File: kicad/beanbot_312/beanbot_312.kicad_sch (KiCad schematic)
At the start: 53 parts, among them M1 P&O2_MEETPUNT, M10 P&O2_RGB_LED, M11 P&O2_RESISTOR, M12 P&O2_MEETPUNT, M13 P&O2_RESISTOR, M14 P&O2_MOSFET, M15 P&O2_RESISTOR, M16 P&O2_ULTRASONE_HC_SR04, M17 P&O2_MEETPUNT, M18 P&O2_MEETPUNT, M19 P&O2_MEETPUNT, M2 P&O2_MEETPUNT, M20 P&O2_MEETPUNT, M21 P&O2_GEWICHTSENSOR2, M22 P&O2_MEETPUNT, M23 P&O2_MEETPUNT, M24 P&O2_MEETPUNT, M25 P&O2_KLEURSENSOR, M26 P&O2_MEETPUNT, M27 P&O2_RELAIS-DP, M28 P&O2_DC-MOTOR, M29 P&O2_RELAIS-DP, M3 P&O2_RESISTOR, M30 P&O2_DC-MOTOR, M31 P&O2_RELAIS-DP, M32 P&O2_DC-MOTOR, M33 P&O2_DIODE, M34 P&O2_DIODE, M35 P&O2_DIODE, M36 P&O2_MEETPUNT, M37 P&O2_MEETPUNT, M38 P&O2_MEETPUNT, M39 P&O2_MEETPUNT, M4 P&O2_MOSFET, M40 P&O2_MEETPUNT, M41 P&O2_MEETPUNT, M42 P&O2_RESISTOR, M43 P&O2_RESISTOR, M44 P&O2_RESISTOR, M45 P&O2_MOSFET, M46 P&O2_MOSFET, M47 P&O2_MOSFET, M48 P&O2_MEETPUNT, M49 P&O2_MEETPUNT, M5 P&O2_RESISTOR, M50 P&O2_MEETPUNT, M51 P&O2_MEETPUNT, M6 P&O2_MEETPUNT, M7 P&O2_RESISTOR, M8 P&O2_MOSFET, M9 P&O2_RESISTOR, U1 P&O2_ARDUINO_MEGA_SHIELD

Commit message: Restore latest version
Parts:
- added M27: P&O2_MEETPUNT, 1_P&O2_lib:P&O2_MEETPUNT, symbol 1_P&O2_lib:P&O2_MEETPUNT
- renumbered M51 to M28, M27 to M29, M28 to M30, M29 to M31, M30 to M32, M31 to M33, M32 to M34, M33 to M35, M34 to M36, M35 to M37, M36 to M38, M37 to M39, M38 to M40, M39 to M41, M40 to M42, M41 to M43, M42 to M44, M43 to M45, M44 to M46, M45 to M47, M46 to M48, M47 to M49, M48 to M50, M49 to M51, M50 to M52
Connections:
- net GND: now also M27.1 (TP)

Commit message: Made outline for pcb
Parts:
- M11, M13, M15, M3, M5, M7, M9: footprint 1_P&O2_lib:P&O2_RES -> 1_P&O2_lib:P&O2_RESISTOR
- SV1: footprint (none) -> 1_P&O2_lib:P&O2_DIP16
- U1: footprint 1_P&O2_lib:P&O2_ARDUINO_MEGA_SHIELD -> (none)
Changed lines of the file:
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@@
       (effects (font (size 1.143 1.143)) (justify left))
     )
-    (property "Footprint" "1_P&O2_lib:P&O2_RES" (id 2) (at 33.02 268.732 0)
+    (property "Footprint" "1_P&O2_lib:P&O2_RESISTOR" (id 2) (at 33.02 268.732 0)
       (effects (font (size 0.508 0.508)) hide)
     )
@@
       (effects (font (size 1.143 1.143)))
     )
-    (property "Footprint" "" (id 2) (at 115.57 189.738 0)
+    (property "Footprint" "1_P&O2_lib:P&O2_DIP16" (id 2) (at 115.57 189.738 0)
       (effects (font (size 0.508 0.508)) hide)
     )
@@
       (effects (font (size 1.143 1.143)))
     )
-    (property "Footprint" "1_P&O2_lib:P&O2_RES" (id 2) (at 85.09 177.038 0)
+    (property "Footprint" "1_P&O2_lib:P&O2_RESISTOR" (id 2) (at 85.09 177.038 0)
       (effects (font (size 0.508 0.508)) hide)
     )
@@
       (effects (font (size 1.143 1.143)) (justify left))
     )
-    (property "Footprint" "1_P&O2_lib:P&O2_RES" (id 2) (at 74.93 244.602 0)
+    (property "Footprint" "1_P&O2_lib:P&O2_RESISTOR" (id 2) (at 74.93 244.602 0)
       (effects (font (size 0.508 0.508)) hide)
     )
@@
       (effects (font (size 1.143 1.143)) (justify left))
     )
-    (property "Footprint" "1_P&O2_lib:P&O2_RES" (id 2) (at 38.1 244.602 0)
+    (property "Footprint" "1_P&O2_lib:P&O2_RESISTOR" (id 2) (at 38.1 244.602 0)
       (effects (font (size 0.508 0.508)) hide)
     )
@@
     (property "Reference" "U1" (id 0) (at 97.155 46.99 0))
     (property "Value" "P&O2_ARDUINO_MEGA_SHIELD" (id 1) (at 97.155 49.53 0))
-    (property "Footprint" "1_P&O2_lib:P&O2_ARDUINO_MEGA_SHIELD" (id 2) (at 49.53 149.86 0)
+    (property "Footprint" "" (id 2) (at 49.53 149.86 0)
       (effects (font (size 1.27 1.27)) hide)
     )
@@
       (effects (font (size 1.143 1.143)) (justify left))
     )
-    (property "Footprint" "1_P&O2_lib:P&O2_RES" (id 2) (at 69.85 268.732 0)
+    (property "Footprint" "1_P&O2_lib:P&O2_RESISTOR" (id 2) (at 69.85 268.732 0)
       (effects (font (size 0.508 0.508)) hide)
     )
@@
       (effects (font (size 1.143 1.143)) (justify left))
     )
-    (property "Footprint" "1_P&O2_lib:P&O2_RES" (id 2) (at 110.49 244.602 0)
+    (property "Footprint" "1_P&O2_lib:P&O2_RESISTOR" (id 2) (at 110.49 244.602 0)
       (effects (font (size 0.508 0.508)) hide)
     )
@@
       (effects (font (size 1.143 1.143)) (justify left))
     )
-    (property "Footprint" "1_P&O2_lib:P&O2_RES" (id 2) (at 105.41 268.732 0)
+    (property "Footprint" "1_P&O2_lib:P&O2_RESISTOR" (id 2) (at 105.41 268.732 0)
       (effects (font (size 0.508 0.508)) hide)
     )
@@
     )
     (path "/14482988-d976-4b64-84c3-34b19aa3c080"
-      (reference "M3") (unit 1) (value "P&O2_RESISTOR") (footprint "1_P&O2_lib:P&O2_RES")
+      (reference "M3") (unit 1) (value "P&O2_RESISTOR") (footprint "1_P&O2_lib:P&O2_RESISTOR")
     )
     (path "/6c971ce3-1431-46f9-8da7-bbee1109d8c7"
@@
     )
     (path "/89a9d6ea-785f-4361-8a21-ea3d7a427841"
-      (reference "M5") (unit 1) (value "P&O2_RESISTOR") (footprint "1_P&O2_lib:P&O2_RES")
+      (reference "M5") (unit 1) (value "P&O2_RESISTOR") (footprint "1_P&O2_lib:P&O2_RESISTOR")
     )
     (path "/27fa6b28-2749-4951-8431-a85c04f7dccf"
@@
     )
     (path "/a9fbfec0-73fe-4272-aeae-3ce0e9053838"
-      (reference "M7") (unit 1) (value "P&O2_RESISTOR") (footprint "1_P&O2_lib:P&O2_RES")
+      (reference "M7") (unit 1) (value "P&O2_RESISTOR") (footprint "1_P&O2_lib:P&O2_RESISTOR")
     )
     (path "/1e4ba2ce-8f73-4698-94a3-6f7c8d2840a2"
@@
     )
     (path "/760a86ab-c275-4512-b55b-15f683b8a6dd"
-      (reference "M9") (unit 1) (value "P&O2_RESISTOR") (footprint "1_P&O2_lib:P&O2_RES")
+      (reference "M9") (unit 1) (value "P&O2_RESISTOR") (footprint "1_P&O2_lib:P&O2_RESISTOR")
     )
     (path "/f3747c8d-50dd-4b9f-b48c-f49fc331b26d"
@@
     )
     (path "/495f9e22-4870-42e2-8c9f-b89669711850"
-      (reference "M11") (unit 1) (value "P&O2_RESISTOR") (footprint "1_P&O2_lib:P&O2_RES")
+      (reference "M11") (unit 1) (value "P&O2_RESISTOR") (footprint "1_P&O2_lib:P&O2_RESISTOR")
     )
     (path "/83e7bd01-8410-4616-9457-7ee77c468abc"
@@
     )
     (path "/f3adaaab-422c-4953-8879-b08863ca4923"
-      (reference "M13") (unit 1) (value "P&O2_RESISTOR") (footprint "1_P&O2_lib:P&O2_RES")
+      (reference "M13") (unit 1) (value "P&O2_RESISTOR") (footprint "1_P&O2_lib:P&O2_RESISTOR")
     )
     (path "/ca63cb53-2ff8-4934-af06-3de3b0c74780"
@@
     )
     (path "/baab9130-8189-4ac5-bff7-a58ac8995f3b"
-      (reference "M15") (unit 1) (value "P&O2_RESISTOR") (footprint "1_P&O2_lib:P&O2_RES")
+      (reference "M15") (unit 1) (value "P&O2_RESISTOR") (footprint "1_P&O2_lib:P&O2_RESISTOR")
     )
     (path "/524c9472-4b27-4e81-93fa-4ac570aaef19"
@@
     )
     (path "/31e61e3b-86e2-42f7-90c4-159698048ccb"
-      (reference "SV1") (unit 1) (value "P&O2_LCD") (footprint "")
+      (reference "SV1") (unit 1) (value "P&O2_LCD") (footprint "1_P&O2_lib:P&O2_DIP16")
     )
     (path "/93bc6bf3-eadd-4f0c-82a1-9da79f283ddb"
-      (reference "U1") (unit 1) (value "P&O2_ARDUINO_MEGA_SHIELD") (footprint "1_P&O2_lib:P&O2_ARDUINO_MEGA_SHIELD")
-    )
-  )
+      (reference "U1") (unit 1) (value "P&O2_ARDUINO_MEGA_SHIELD") (footprint "")
+    )
+  )

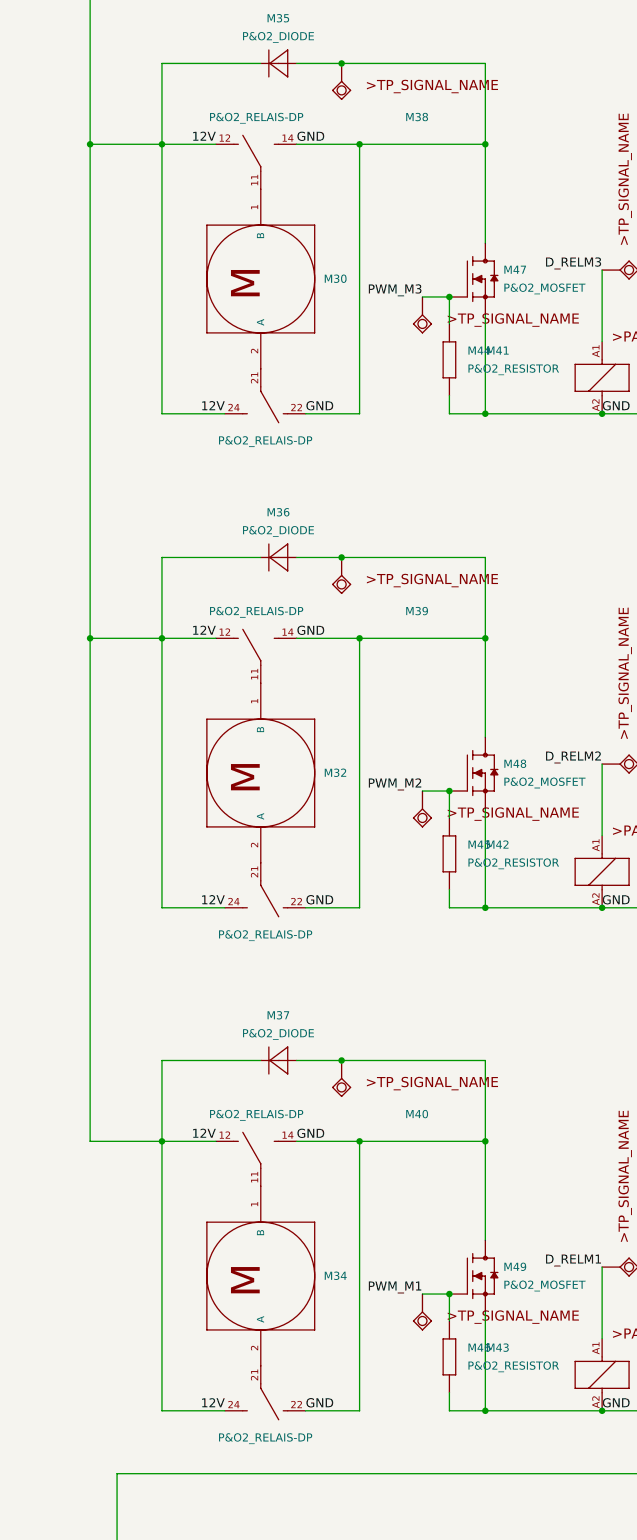
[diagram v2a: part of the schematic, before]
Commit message: First attempt for DC motor & tweaked scheme a little
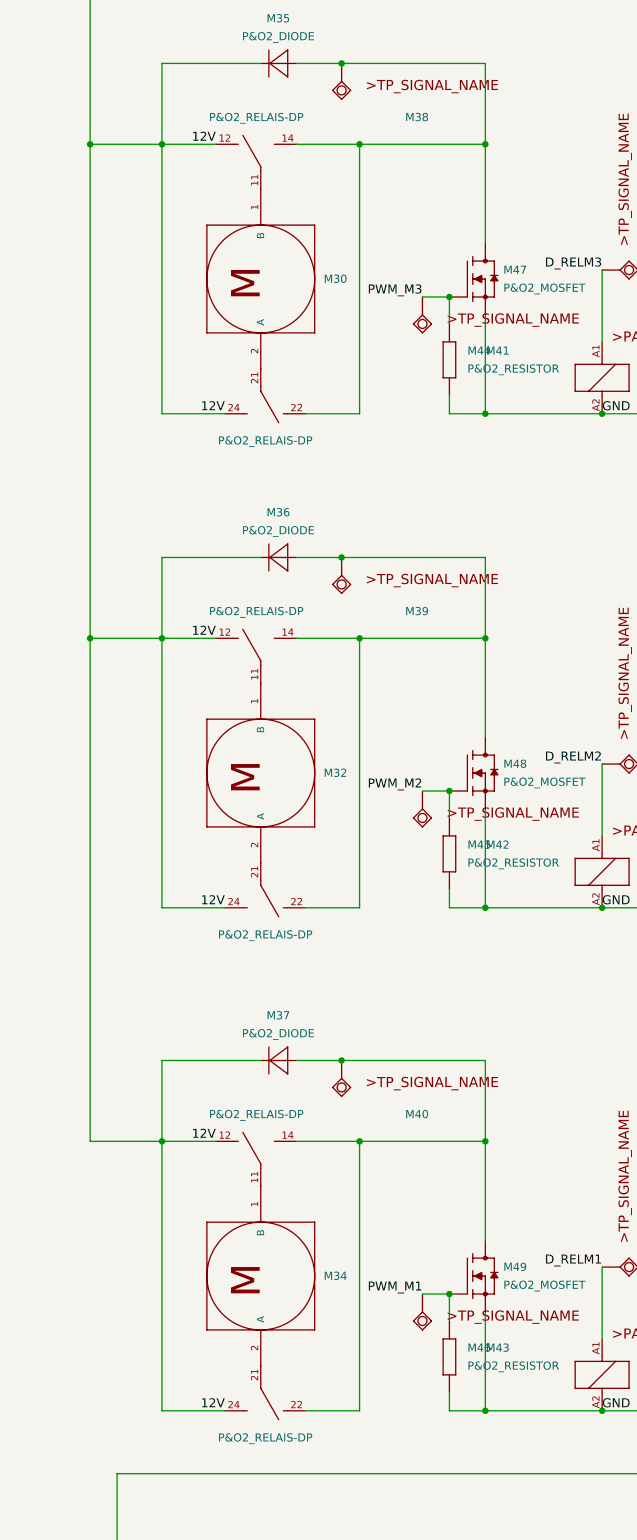
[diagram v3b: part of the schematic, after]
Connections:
- net GND: no longer M29.14 (1), M29.22 (1), M31.14 (1), M31.22 (1), M33.14 (1), M33.22 (1), M35.A, M36.A, M37.A, M38.1 (TP), M39.1 (TP), M40.1 (TP), M47.2 (D), M48.2 (D), M49.2 (D)
- new net: M29.14 (1), M29.22 (1), M35.A, M38.1 (TP), M47.2 (D)
- new net: M33.14 (1), M33.22 (1), M37.A, M40.1 (TP), M49.2 (D)
- new net: M31.14 (1), M31.22 (1), M36.A, M39.1 (TP), M48.2 (D)
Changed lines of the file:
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@@
     (effects (font (size 1.27 1.27)) (justify right bottom))
-  )
-  (label "GND" (at 317.5 162.56 0)
-    (effects (font (size 1.27 1.27)) (justify left bottom))
   )
   (label "5V" (at 121.92 165.1 0)
@@
     (effects (font (size 1.27 1.27)) (justify left bottom))
   )
-  (label "GND" (at 317.5 233.68 0)
-    (effects (font (size 1.27 1.27)) (justify left bottom))
-  )
   (label "5V" (at 146.05 223.52 0)
     (effects (font (size 1.27 1.27)) (justify left bottom))
@@
     (effects (font (size 1.27 1.27)) (justify right bottom))
   )
-  (label "GND" (at 317.5 92.71 0)
-    (effects (font (size 1.27 1.27)) (justify left bottom))
-  )
-  (label "GND" (at 316.23 195.58 0)
-    (effects (font (size 1.27 1.27)) (justify left bottom))
-  )
   (label "D_LCDE" (at 111.76 182.88 90)
     (effects (font (size 1.27 1.27)) (justify left bottom))
@@
     (effects (font (size 1.27 1.27)) (justify left bottom))
   )
-  (label "GND" (at 316.23 124.46 0)
-    (effects (font (size 1.27 1.27)) (justify left bottom))
-  )
   (label "PWM_LEDR" (at 25.4 256.54 180)
     (effects (font (size 1.27 1.27)) (justify right bottom))
@@
     (effects (font (size 1.27 1.27)) (justify left bottom))
   )
-  (label "GND" (at 316.23 54.61 0)
-    (effects (font (size 1.27 1.27)) (justify left bottom))
-  )

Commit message: Almost finished
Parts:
- removed M22: P&O2_MEETPUNT, 1_P&O2_lib:P&O2_MEETPUNT, symbol 1_P&O2_lib:P&O2_MEETPUNT
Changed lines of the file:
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@@
   (junction (at 25.4 223.52) (diameter 0) (color 0 0 0 0)
   )
-  (junction (at 231.14 257.81) (diameter 0) (color 0 0 0 0)
-  )
   (junction (at 342.9 162.56) (diameter 0) (color 0 0 0 0)
   )
@@
     (stroke (width 0) (type default) (color 0 0 0 0))
   )
-  (wire (pts (xy 231.14 257.81) (xy 231.14 223.52))
+  (wire (pts (xy 231.14 223.52) (xy 231.14 262.89))
     (stroke (width 0) (type default) (color 0 0 0 0))
   )
@@
   )
   (wire (pts (xy 29.21 276.86) (xy 34.29 276.86))
-    (stroke (width 0) (type default) (color 0 0 0 0))
-  )
-  (wire (pts (xy 231.14 262.89) (xy 231.14 257.81))
     (stroke (width 0) (type default) (color 0 0 0 0))
   )
@@
     (pin "1")
     (pin "2")
-  )
-  (symbol (lib_id "1_P&O2_lib:P&O2_MEETPUNT") (at 233.68 257.81 90) (unit 1)
-    (in_bom yes) (on_board yes) (fields_autoplaced)
-    (property "Reference" "M22" (id 0) (at 237.49 247.1568 90)
-      (effects (font (size 1.143 1.143)) (justify right))
-    )
-    (property "Value" "P&O2_MEETPUNT" (id 1) (at 233.68 257.81 0)
-      (effects (font (size 1.143 1.143)) (justify left bottom) hide)
-    )
-    (property "Footprint" "1_P&O2_lib:P&O2_MEETPUNT" (id 2) (at 229.87 257.048 0)
-      (effects (font (size 0.508 0.508)) hide)
-    )
-    (property "Datasheet" "" (id 3) (at 233.68 257.81 0)
-      (effects (font (size 1.27 1.27)) hide)
-    )
-    (pin "1")
   )
   (symbol (lib_id "1_P&O2_lib:P&O2_RESISTOR") (at 71.12 243.84 270) (unit 1)
@@
       (reference "M21") (unit 1) (value "P&O2_GEWICHTSENSOR2") (footprint "1_P&O2_lib:P&O2_GEWICHTSENSOR-4PIN")
     )
-    (path "/7560bc7c-edc7-4ac6-9493-a5066a60c8ba"
-      (reference "M22") (unit 1) (value "P&O2_MEETPUNT") (footprint "1_P&O2_lib:P&O2_MEETPUNT")
-    )
     (path "/d268de9b-047a-4a0e-a97d-30f342894d7b"

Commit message: Added footprints
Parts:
- SV1: footprint 1_P&O2_lib:P&O2_DIP16 -> 1_P&O2_lib:P&O2_LCD
- U1: footprint (none) -> 1_P&O2_lib:P&O2_ARDUINO_MEGA_SHIELD
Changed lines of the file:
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@@
       (effects (font (size 1.143 1.143)))
     )
-    (property "Footprint" "1_P&O2_lib:P&O2_DIP16" (id 2) (at 115.57 189.738 0)
+    (property "Footprint" "1_P&O2_lib:P&O2_LCD" (id 2) (at 115.57 189.738 0)
       (effects (font (size 0.508 0.508)) hide)
     )
@@
     (property "Reference" "U1" (id 0) (at 97.155 46.99 0))
     (property "Value" "P&O2_ARDUINO_MEGA_SHIELD" (id 1) (at 97.155 49.53 0))
-    (property "Footprint" "" (id 2) (at 49.53 149.86 0)
+    (property "Footprint" "1_P&O2_lib:P&O2_ARDUINO_MEGA_SHIELD" (id 2) (at 49.53 149.86 0)
       (effects (font (size 1.27 1.27)) hide)
     )
@@
     )
     (path "/31e61e3b-86e2-42f7-90c4-159698048ccb"
-      (reference "SV1") (unit 1) (value "P&O2_LCD") (footprint "1_P&O2_lib:P&O2_DIP16")
+      (reference "SV1") (unit 1) (value "P&O2_LCD") (footprint "1_P&O2_lib:P&O2_LCD")
     )
     (path "/93bc6bf3-eadd-4f0c-82a1-9da79f283ddb"
-      (reference "U1") (unit 1) (value "P&O2_ARDUINO_MEGA_SHIELD") (footprint "")
-    )
-  )
+      (reference "U1") (unit 1) (value "P&O2_ARDUINO_MEGA_SHIELD") (footprint "1_P&O2_lib:P&O2_ARDUINO_MEGA_SHIELD")
+    )
+  )

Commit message: Updated pcb
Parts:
- removed M33: P&O2_RELAIS-DP, 1_P&O2_lib:P&O2_RELAY-DP, symbol 1_P&O2_lib:P&O2_RELAIS-DP
- removed M34: P&O2_DC-MOTOR, 1_P&O2_lib:P&O2_2PIN-SCREW-5.08, symbol 1_P&O2_lib:P&O2_DC-MOTOR
- removed M37: P&O2_DIODE, 1_P&O2_lib:P&O2_DIODE, symbol 1_P&O2_lib:P&O2_DIODE
- removed M40, M43, M52: P&O2_MEETPUNT, 1_P&O2_lib:P&O2_MEETPUNT, symbol 1_P&O2_lib:P&O2_MEETPUNT
- removed M46: P&O2_RESISTOR, 1_P&O2_lib:P&O2_RESISTOR, symbol 1_P&O2_lib:P&O2_RESISTOR
- removed M49: P&O2_MOSFET, 1_P&O2_lib:P&O2_TO220, symbol 1_P&O2_lib:P&O2_MOSFET
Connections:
- net D_RELM1 is gone; now on net D_RELM2: U1.58 (D24)
- net D_KOUT: now also U1.64 (D38); no longer U1.60 (RX1)
- net D_KS2: now also U1.62 (TX3); no longer U1.28 (RX2)
- net D_KS3: now also U1.60 (RX1); no longer U1.59 (TX1)
- net D_RELM2: no longer U1.57 (D26)
- net D_RELM3: now also U1.57 (D26); no longer U1.27 (D27)
- net D_UECHO: now also U1.28 (RX2); no longer U1.62 (TX3)
- net PWM_LEDB: now also U1.22 (D13); no longer U1.30 (D11)
- net PWM_LEDG: now also U1.24 (D12); no longer U1.32 (D10)
- net PWM_LEDR: now also U1.30 (D11); no longer U1.21 (D9)
- net PWM_M2: now also U1.56 (D7); no longer U1.29 (D3)
- net PWM_M3: now also U1.55 (D6); no longer U1.42 (D4)
- net PWM_M1: no longer names the net of U1.31 (D2)

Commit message: Some progress on the PCB
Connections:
- net D_LCDDB4: now also U1.47 (D46); no longer U1.51 (D50)
- net D_LCDDB5: now also U1.45 (D52); no longer U1.52 (D51)
- net D_LCDDB6: now also U1.43 (D47); no longer U1.45 (D52)
- net D_LCDDB7: now also U1.41 (D45); no longer U1.46 (D53)
- net D_LCDRS: now also U1.51 (D50); no longer U1.50 (D48)
- net PWM_UTRIG: now also U1.32 (D10); no longer U1.23 (D8)
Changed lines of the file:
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@@
     (effects (font (size 1.27 1.27)) (justify right bottom))
+  )
+  (label "D_LCDDB4" (at 142.24 104.14 0)
+    (effects (font (size 1.27 1.27)) (justify left bottom))
   )
   (label "D_RELM2" (at 359.41 142.24 180)
@@
     (effects (font (size 1.27 1.27)) (justify right bottom))
   )
+  (label "PWM_UTRIG" (at 116.84 148.59 180)
+    (effects (font (size 1.27 1.27)) (justify right bottom))
+  )
   (label "12V" (at 306.07 162.56 180)
     (effects (font (size 1.27 1.27)) (justify right bottom))
@@
   (label "GND" (at 359.41 92.71 0)
     (effects (font (size 1.27 1.27)) (justify left bottom))
-  )
-  (label "D_LCDDB4" (at 142.24 114.3 0)
-    (effects (font (size 1.27 1.27)) (justify left bottom))
-  )
-  (label "D_LCDDB5" (at 116.84 114.3 180)
-    (effects (font (size 1.27 1.27)) (justify right bottom))
   )
   (label "5V" (at 121.92 165.1 0)
@@
     (effects (font (size 1.27 1.27)) (justify left bottom))
   )
-  (label "D_LCDDB7" (at 116.84 99.06 180)
-    (effects (font (size 1.27 1.27)) (justify right bottom))
-  )
   (label "PWM_UTRIG" (at 162.56 237.49 0)
     (effects (font (size 1.27 1.27)) (justify left bottom))
@@
     (effects (font (size 1.27 1.27)) (justify left bottom))
   )
+  (label "D_LCDRS" (at 142.24 114.3 0)
+    (effects (font (size 1.27 1.27)) (justify left bottom))
+  )
   (label "12V" (at 304.8 54.61 180)
-    (effects (font (size 1.27 1.27)) (justify right bottom))
-  )
-  (label "D_LCDRS" (at 116.84 109.22 180)
     (effects (font (size 1.27 1.27)) (justify right bottom))
   )
@@
   )
   (label "GND" (at 71.12 276.86 0)
+    (effects (font (size 1.27 1.27)) (justify left bottom))
+  )
+  (label "D_LCDDB5" (at 142.24 99.06 0)
     (effects (font (size 1.27 1.27)) (justify left bottom))
   )
@@
   (label "PWM_LEDR" (at 116.84 143.51 180)
     (effects (font (size 1.27 1.27)) (justify right bottom))
-  )
-  (label "PWM_UTRIG" (at 142.24 128.27 0)
-    (effects (font (size 1.27 1.27)) (justify left bottom))
   )
   (label "GND" (at 34.29 276.86 0)
@@
     (effects (font (size 1.27 1.27)) (justify left bottom))
   )
+  (label "D_LCDDB7" (at 142.24 88.9 0)
+    (effects (font (size 1.27 1.27)) (justify left bottom))
+  )
   (label "D_LCDDB7" (at 91.44 182.88 90)
     (effects (font (size 1.27 1.27)) (justify left bottom))
   )
-  (label "D_LCDDB6" (at 142.24 99.06 0)
+  (label "D_LCDDB6" (at 142.24 93.98 0)
     (effects (font (size 1.27 1.27)) (justify left bottom))
   )
